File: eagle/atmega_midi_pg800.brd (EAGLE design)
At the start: 100 x 80 mm, 39 parts, among them IC1 78L05Z, IC2 4067N, IC3 4067N, IC4 4067N, Q1 16.000Mhz, U1 6N138, U2 ATMEGA328P_PDIP, X1 MAB6H

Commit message: standard connector for display
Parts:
- DISPLAY: value (none) -> 22-23-2041; device SparkFun-Connectors:MOLEX-1X4 -> con-molex:22-23-2041
- moved IN13 9.25 mm to (71.1, 45.7), turned to 270 degrees
- moved IN14 9.25 mm to (38.1, 45.7), turned to 270 degrees
- moved IN15 9.25 mm to (3.81, 45.7), turned to 270 degrees
- moved IC1 5.39 mm to (49.5, 19.1)
- moved DISPLAY 1.27 mm to (10.2, 36.8)
- moved IN16 1.27 mm to (76.2, 33.0)
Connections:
- net +5V: now also DISPLAY.4; no longer DISPLAY.1
- net GND: now also DISPLAY.3; no longer DISPLAY.2
- net N$12: now also DISPLAY.2; no longer DISPLAY.3
- net N$13: now also DISPLAY.1; no longer DISPLAY.4
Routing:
- net GND: track 210.5 -> 198.7 mm
- net +5V: track 78.9 -> 71.1 mm

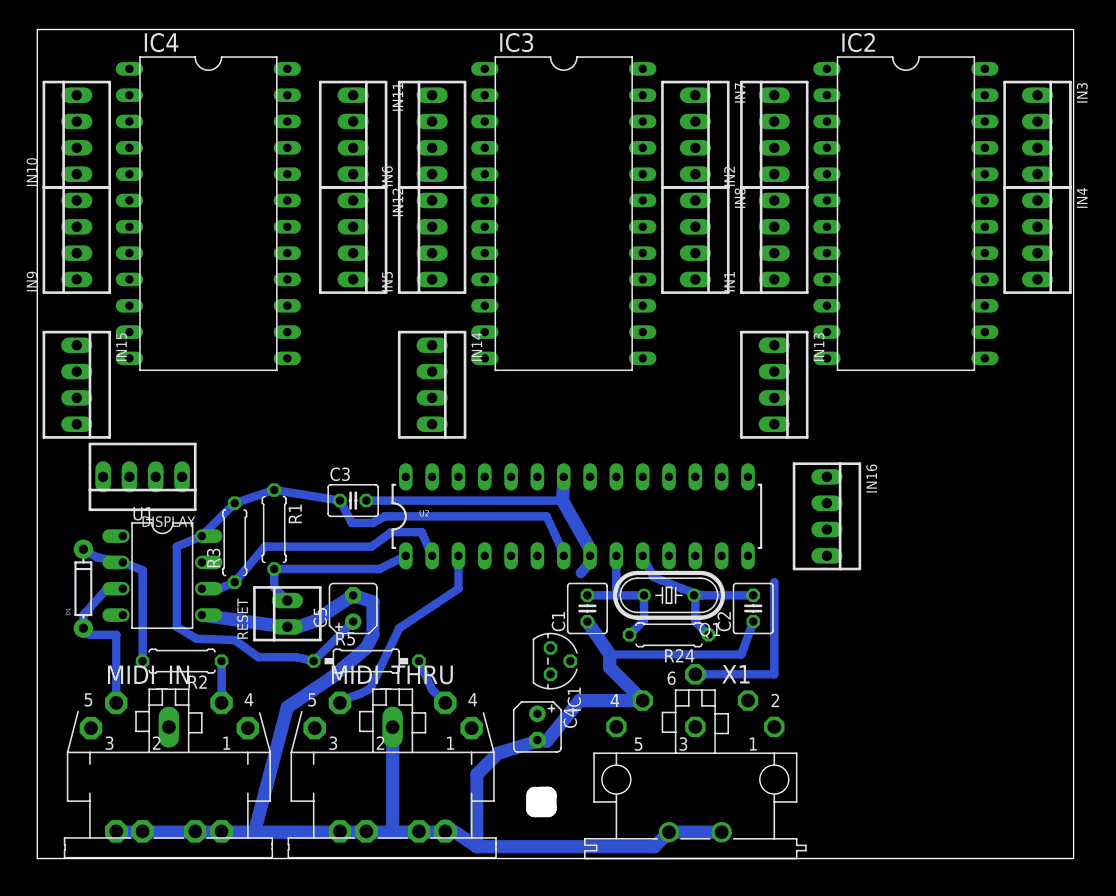
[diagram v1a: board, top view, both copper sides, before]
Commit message: rotary encoder connection
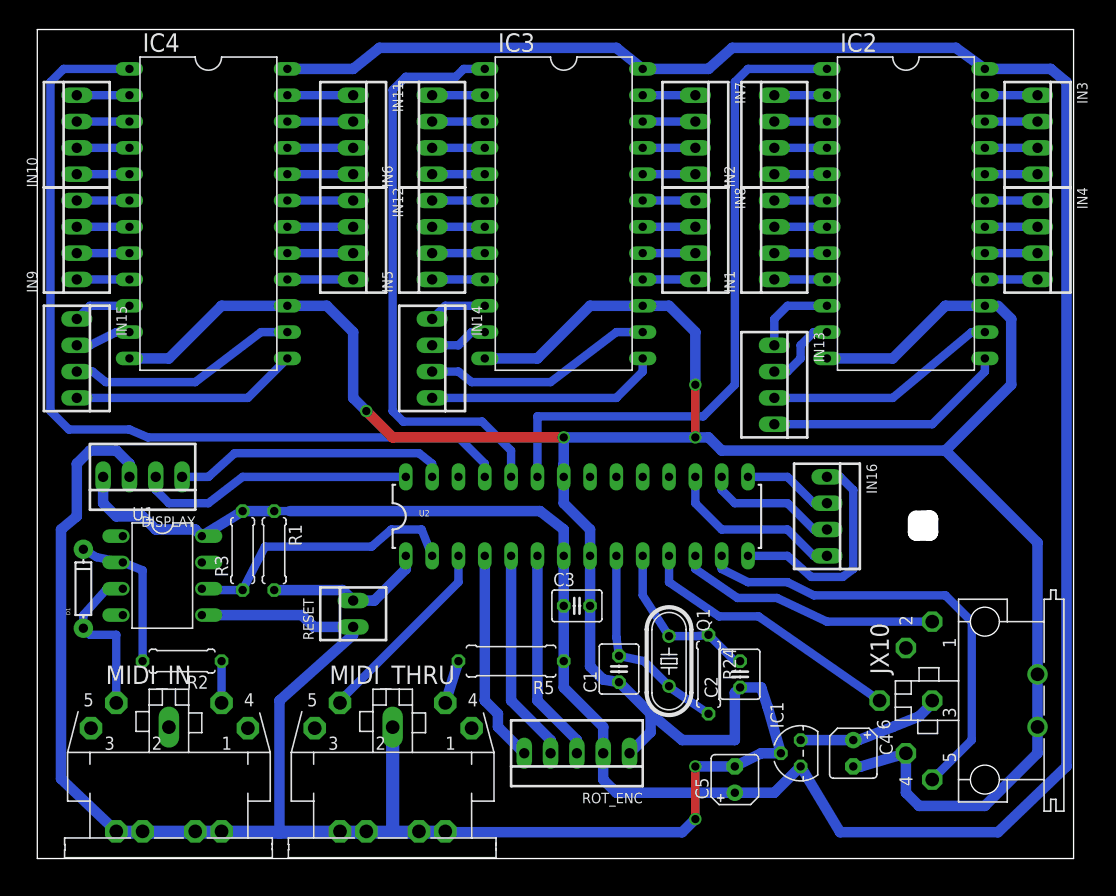
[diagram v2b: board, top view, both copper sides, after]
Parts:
- removed X1: MAB6H, con-hirschmann:MAB6H
- added JX10: MAB6H, con-hirschmann:MAB6H
- added ROT_ENC: 22-23-2051, con-molex:22-23-2051
- R5: device rcl:0207/10 -> rcl:0309/10
- moved C5 40.4 mm to (67.3, 7.62)
- moved C4 30.6 mm to (78.7, 10.2)
- moved IC1 25.7 mm to (73.7, 10.2), turned to 90 degrees
- moved C3 23.9 mm to (52.1, 24.4)
- moved R5 14.0 mm to (45.7, 19.1), turned to 180 degrees
- moved C1 6.59 mm to (56.1, 18.3)
- moved C2 6.48 mm to (67.8, 17.8)
- moved RESET 6.35 mm to (30.5, 23.6)
- moved Q1 6.35 mm to (61.0, 19.1), turned to 270 degrees
- moved R24 5.39 mm to (64.8, 17.8), turned to 270 degrees
- moved IN14 2.54 mm to (38.1, 48.3)
- moved IN15 2.54 mm to (3.81, 48.3)
- moved R1 2.03 mm to (22.9, 29.7)
- moved R3 1.08 mm to (19.8, 29.7)
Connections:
- removed net VDD: IC2.24, IC3.24, IC4.24
- removed net VSS: IC2.12, IC3.12, IC4.12
- new net N$84: ROT_ENC.5, U2.4
- new net N$85: ROT_ENC.4, U2.5
- new net N$86: ROT_ENC.3, U2.6
- net +5V: now also IC2.24, IC3.24, IC4.24, ROT_ENC.2
- net GND: now also IC2.12, IC3.12, IC4.12, JX10.4, JX10.PE, JX10.PE@, ROT_ENC.1; no longer X1.4, X1.PE, X1.PE@
- net N$10: now also JX10.1, U2.12; no longer U2.11, X1.1
- net N$11: now also JX10.5; no longer X1.5
- net N$6: now also JX10.3; no longer X1.3
- net N$9: now also JX10.6, U2.11; no longer U2.12, X1.6
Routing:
- net GND: track 198.7 -> 444.7 mm, vias 0 -> 6
- net +5V: track 71.1 -> 273.3 mm
- net N$2: track 0.00 -> 85.0 mm
- net N$15: track 0.00 -> 64.8 mm
- net N$14: track 0.00 -> 56.3 mm
- net N$11: track 0.00 -> 43.9 mm
- net N$12: track 0.00 -> 26.8 mm
- net N$13: track 0.00 -> 26.6 mm
- net N$10: track 0.00 -> 25.5 mm
- net N$80: track 0.00 -> 23.7 mm
- net N$72: track 0.00 -> 22.6 mm
- net N$81: track 0.00 -> 22.6 mm
- net N$71: track 0.00 -> 22.3 mm
- net N$75: track 0.00 -> 22.3 mm
- net N$76: track 0.00 -> 21.9 mm
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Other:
- outline, holes or cut-outs redrawn

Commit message: cutout
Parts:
- moved IN13 2.54 mm to (71.1, 48.3)
- moved R2 2.05 mm to (11.9, 18.8)
- moved C3 1.27 mm to (52.1, 25.7)
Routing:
- net GND: track 444.7 -> 434.4 mm
- net N$83: track 8.15 -> 5.61 mm
- net N$82: track 7.40 -> 5.38 mm
- net N$80: track 23.7 -> 21.9 mm
- net N$7: track 14.9 -> 16.6 mm
- net +5V: track 273.3 -> 271.7 mm
- net N$3: track 16.2 -> 15.1 mm
- net N$72: track 22.6 -> 21.6 mm
- net N$2: track 85.0 -> 85.8 mm
- net N$15: track 64.8 -> 64.0 mm
- net N$43: track 15.7 -> 14.9 mm
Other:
- board size 100 x 80 mm -> 101.9 x 80.8 mm

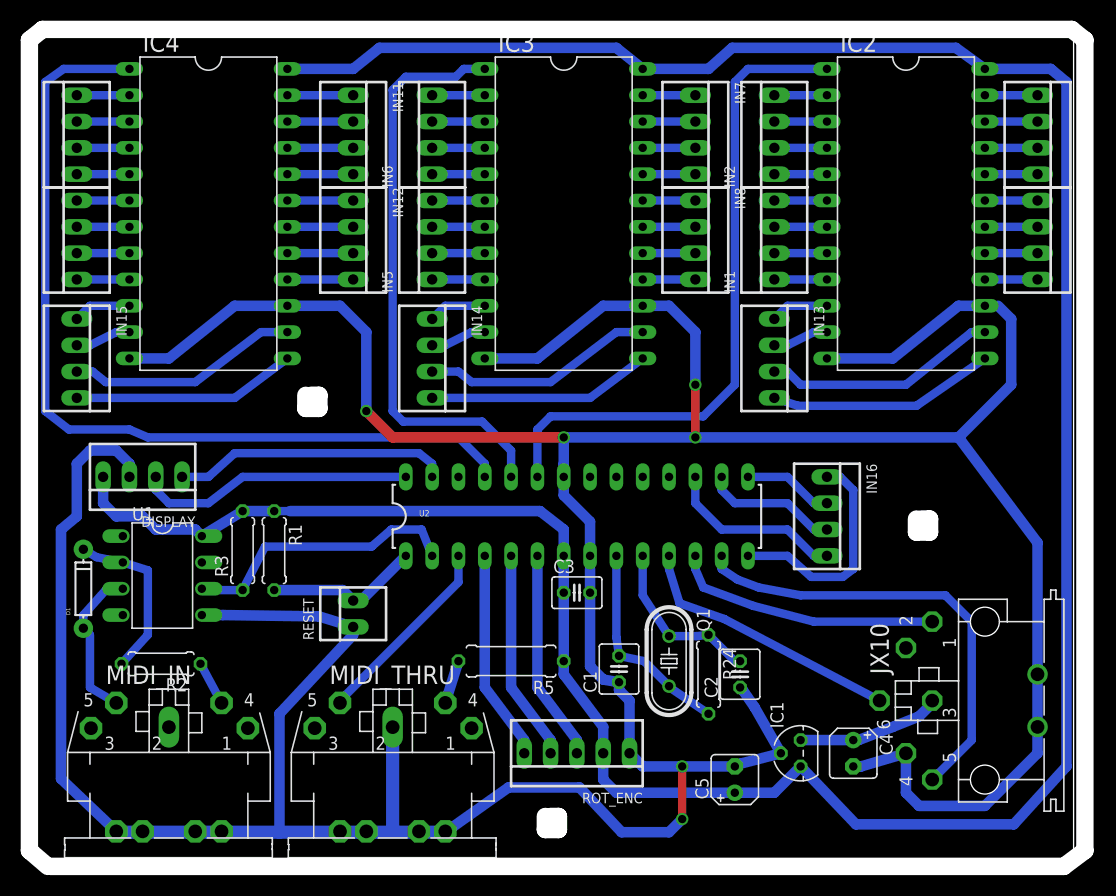
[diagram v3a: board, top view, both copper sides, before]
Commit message: big boy version of 7805 to power those 4067 and the display
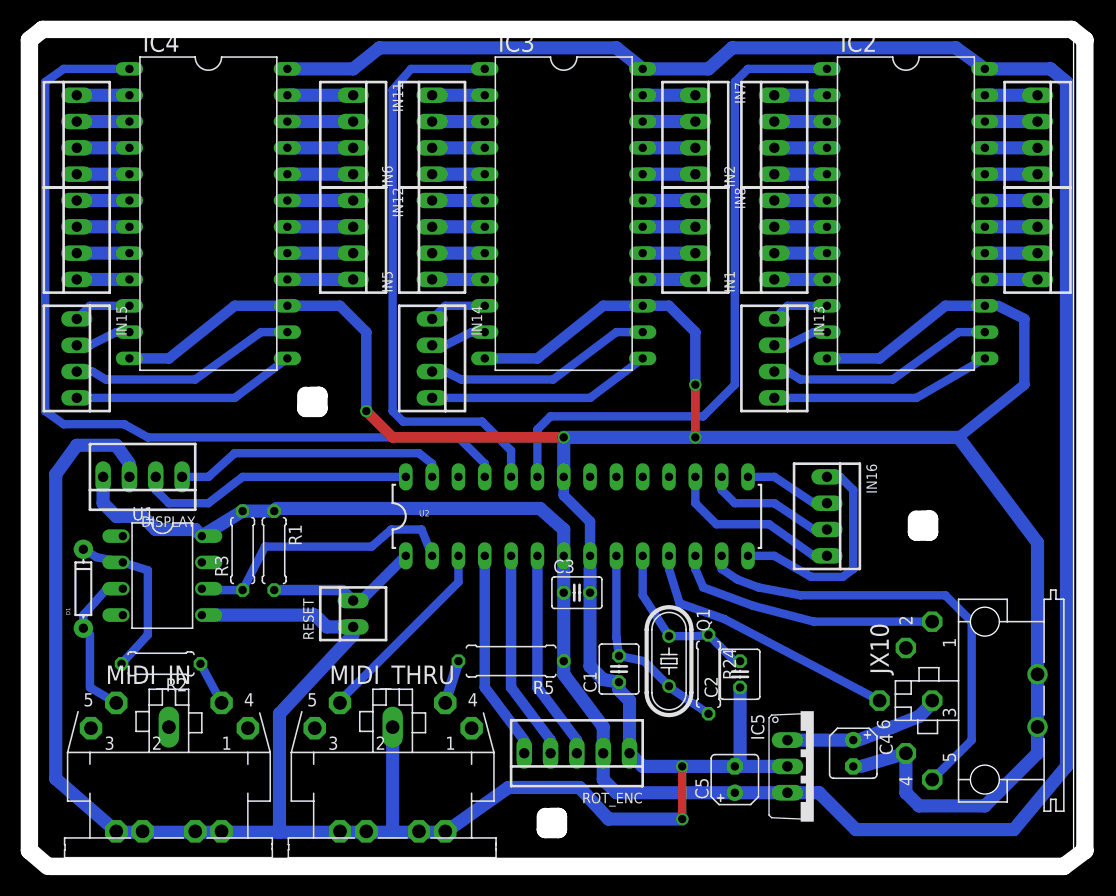
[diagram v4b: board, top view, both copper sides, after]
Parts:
- removed IC1: 78L05Z, linear:TO92
- added IC5: 7805TV, linear:TO220V
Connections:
- net +5V: now also IC5.3; no longer IC1.1
- net GND: now also IC5.2; no longer IC1.2
- net N$6: now also IC5.1; no longer IC1.3
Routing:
- net GND: track 434.4 -> 439.0 mm
- net +5V: track 271.7 -> 270.4 mm
- net N$6: track 13.9 -> 15.2 mm
- net N$81: track 22.6 -> 22.0 mm
- net N$80: track 21.9 -> 21.3 mm

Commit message: protectoin diode and pot power hookups
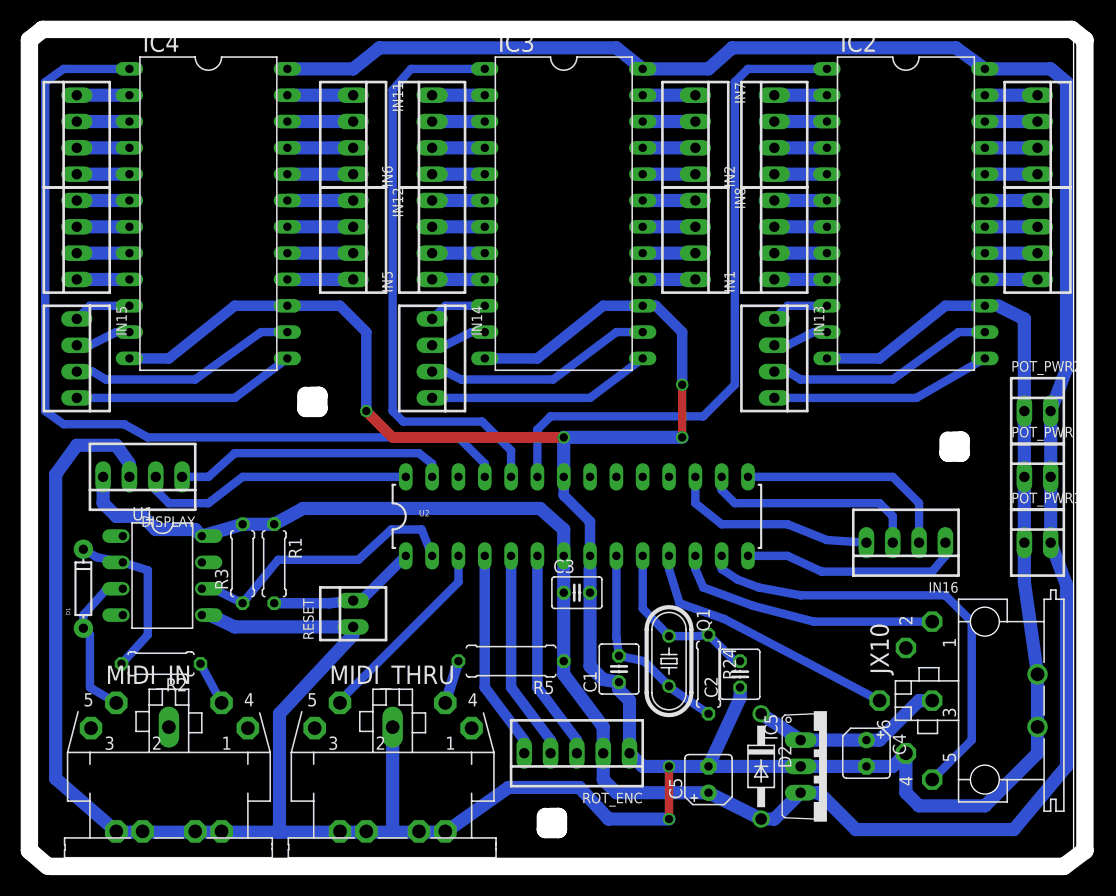
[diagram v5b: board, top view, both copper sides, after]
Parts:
- added D2: 1N4004, diode:DO41-10
- added POT_PWR, POT_PWR1, POT_PWR2: 22-23-2021, con-molex:22-23-2021
- moved IN16 8.03 mm to (83.8, 30.5), turned to 180 degrees
- moved C5 2.54 mm to (64.8, 7.62)
- moved C4 1.27 mm to (80.0, 10.2)
- moved R1 1.27 mm to (22.9, 28.4)
- moved R3 1.27 mm to (19.8, 28.4)
- moved IC5 1.27 mm to (76.2, 8.89)
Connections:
- net +5V: now also D2.A, POT_PWR.2, POT_PWR1.2, POT_PWR2.2
- net GND: now also POT_PWR.1, POT_PWR1.1, POT_PWR2.1
- net N$6: now also D2.C
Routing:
- net GND: track 439.0 -> 410.6 mm
- net N$17: track 8.39 -> 21.4 mm
- net N$77: track 12.7 -> 21.4 mm
- net N$6: track 15.2 -> 18.9 mm
- net N$78: track 17.0 -> 20.1 mm
- net +5V: track 270.4 -> 272.4 mm
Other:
- outline, holes or cut-outs redrawn
